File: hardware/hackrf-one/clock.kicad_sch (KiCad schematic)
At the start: 67 parts, among them P1 AD_CLK, P16 CLKIN, P2 CLKOUT, P21 MIX_CLK, P37 SCL, P38 SDA, P57 XCVR_CLK, P59 GCK2, P60 SGPIO_CLK, P72 GP_CLKIN, P8 FSX2_CLK, U16 74LVC1G3157, U19 Si5351A-B-GT, U22 74LVC1G80, U26 74AUP2G58GU, U27 74AUP2G58GU, U28 74AUP2G58GU, U29 74AUP2G58GU, X1 GSG-XTAL4PIN

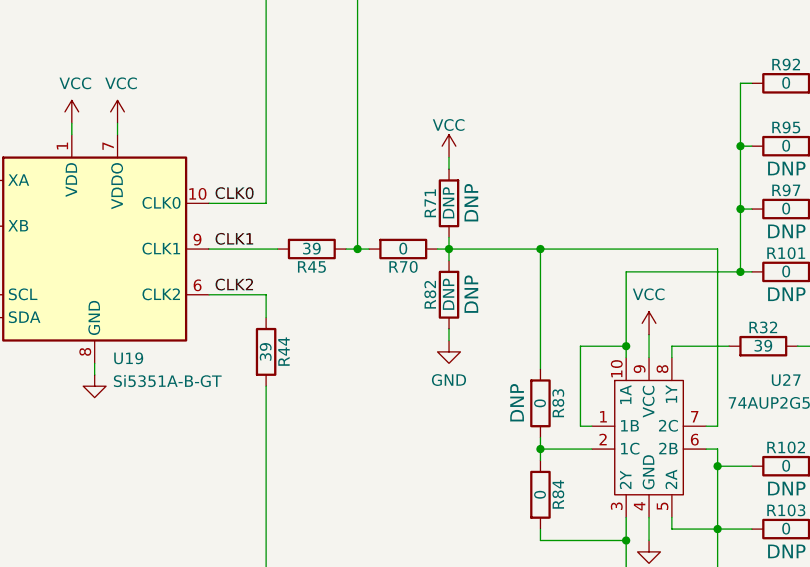
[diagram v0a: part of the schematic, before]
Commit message: HackRF One: adjust clock phase with RC delay
Remove chaining of buffers to delay GCK2 and instead use an RC delay for
both GCK2 and SGPIO_CLK.
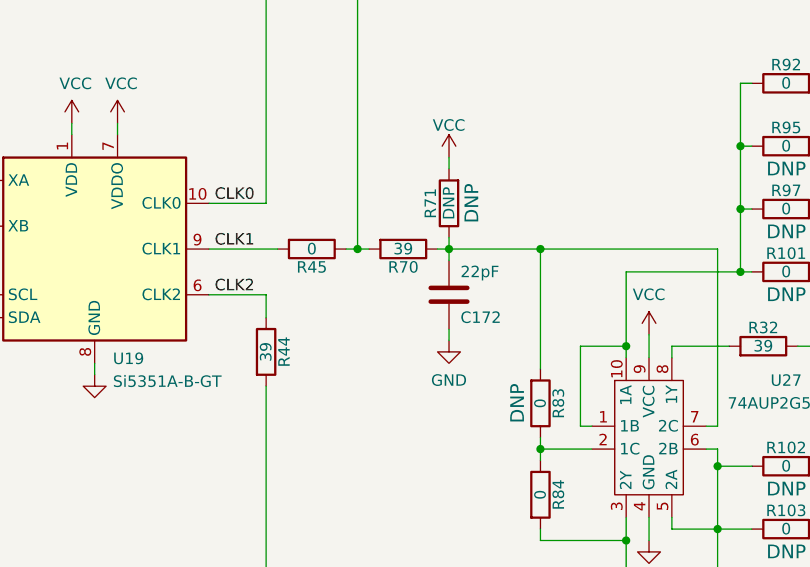
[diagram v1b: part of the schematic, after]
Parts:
- removed R82: DNP, hackrf:GSG-0402, symbol Device:R
- added C172: 22pF, hackrf:GSG-0402, symbol Device:C
- R45: value 39 -> 0; Part Number RMCF0402JT39R0 -> RMCF0402ZT0R00
- R70: value 0 -> 39; Part Number RMCF0402ZT0R00 -> RMCF0402JT39R0
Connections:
- net GND: now also C172.1
- net at R70.1, R71.1, R83.2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: now also C172.2
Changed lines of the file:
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@@
     (in_bom yes) (on_board yes)
     (property "Reference" "R70" (id 0) (at 272.415 94.107 90))
-    (property "Value" "0" (id 1) (at 272.415 92.075 90))
+    (property "Value" "39" (id 1) (at 272.415 92.075 90))
     (property "Footprint" "hackrf:GSG-0402" (id 2) (at 272.415 92.075 0)
       (effects (font (size 1.524 1.524)) hide)
@@
       (effects (font (size 1.524 1.524)) hide)
     )
-    (property "Part Number" "RMCF0402ZT0R00" (id 5) (at 272.415 92.075 0)
-      (effects (font (size 1.524 1.524)) hide)
-    )
-    (property "Description" "RES 0.0 OHM 1/16W 0402 SMD" (id 6) (at 272.415 92.075 0)
+    (property "Part Number" "RMCF0402JT39R0" (id 5) (at 272.415 92.075 0)
+      (effects (font (size 1.524 1.524)) hide)
+    )
+    (property "Description" "RES 39 OHM 1/16W 5% 0402 SMD" (id 6) (at 272.415 92.075 0)
       (effects (font (size 1.524 1.524)) hide)
     )
@@
     (in_bom yes) (on_board yes)
     (property "Reference" "R45" (id 0) (at 262.255 94.107 90))
-    (property "Value" "39" (id 1) (at 262.255 92.075 90))
+    (property "Value" "0" (id 1) (at 262.255 92.075 90))
     (property "Footprint" "hackrf:GSG-0402" (id 2) (at 262.255 92.075 0)
       (effects (font (size 1.524 1.524)) hide)
@@
       (effects (font (size 1.524 1.524)) hide)
     )
-    (property "Part Number" "RMCF0402JT39R0" (id 5) (at 262.255 92.075 0)
-      (effects (font (size 1.524 1.524)) hide)
-    )
-    (property "Description" "RES 39 OHM 1/16W 5% 0402 SMD" (id 6) (at 262.255 92.075 0)
+    (property "Part Number" "RMCF0402ZT0R00" (id 5) (at 262.255 92.075 0)
+      (effects (font (size 1.524 1.524)) hide)
+    )
+    (property "Description" "RES 0.0 OHM 1/16W 0402 SMD" (id 6) (at 262.255 92.075 0)
       (effects (font (size 1.524 1.524)) hide)
     )
@@
     (pin "1")
   )
-  (symbol (lib_id "Device:R") (at 277.495 97.155 180) (unit 1)
-    (in_bom yes) (on_board yes)
-    (property "Reference" "R82" (id 0) (at 275.463 97.155 90))
-    (property "Value" "DNP" (id 1) (at 277.495 97.155 90))
-    (property "Footprint" "hackrf:GSG-0402" (id 2) (at 277.495 97.155 0)
-      (effects (font (size 1.524 1.524)) hide)
-    )
-    (property "Datasheet" "" (id 3) (at 277.495 97.155 0)
-      (effects (font (size 1.524 1.524)))
-    )
-    (property "DNP" "DNP" (id 4) (at 280.035 97.155 90)
-      (effects (font (size 1.524 1.524)))
-    )
-    (pin "1")
-    (pin "2")
-  )
   (symbol (lib_id "Connector_Generic:Conn_01x01") (at 62.23 190.5 90) (unit 1)
     (in_bom yes) (on_board yes)
@@
     (pin "1")
   )
+  (symbol (lib_id "Device:C") (at 277.495 97.155 0) (mirror x) (unit 1)
+    (in_bom yes) (on_board yes)
+    (property "Reference" "C172" (id 0) (at 278.765 99.695 0)
+      (effects (font (size 1.27 1.27)) (justify left))
+    )
+    (property "Value" "22pF" (id 1) (at 278.765 94.615 0)
+      (effects (font (size 1.27 1.27)) (justify left))
+    )
+    (property "Footprint" "hackrf:GSG-0402" (id 2) (at 277.495 97.155 0)
+      (effects (font (size 1.524 1.524)) hide)
+    )
+    (property "Datasheet" "" (id 3) (at 277.495 97.155 0)
+      (effects (font (size 1.524 1.524)) hide)
+    )
+    (property "Manufacturer" "Samsung" (id 4) (at 286.385 100.965 0)
+      (effects (font (size 1.524 1.524)) hide)
+    )
+    (property "Part Number" "CL05C220JB5NNNC" (id 5) (at 286.385 100.965 0)
+      (effects (font (size 1.524 1.524)) hide)
+    )
+    (property "Description" "CAP CER 22PF 50V 5% C0G/NP0 0402" (id 6) (at 286.385 100.965 0)
+      (effects (font (size 1.524 1.524)) hide)
+    )
+    (pin "1")
+    (pin "2")
+  )
   (symbol (lib_id "Device:R") (at 101.6 81.28 0) (unit 1)

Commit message: HackRF One: update 100 nF capacitor part selection
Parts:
- C113, C119, C120, C121, C122, C159, C168, C68, C69: Manufacturer Murata -> Samsung; Part Number GRM155R61A104KA01D -> CL05A104KA5NNNC
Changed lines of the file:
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@@
       (effects (font (size 1.524 1.524)) hide)
     )
-    (property "Manufacturer" "Murata" (id 4) (at 90.805 224.79 0)
-      (effects (font (size 1.524 1.524)) hide)
-    )
-    (property "Part Number" "GRM155R61A104KA01D" (id 5) (at 90.805 224.79 0)
-      (effects (font (size 1.524 1.524)) hide)
-    )
-    (property "Description" "CAP CER 0.1UF 10V 10% X5R 0402" (id 6) (at 90.805 224.79 0)
+    (property "Manufacturer" "Samsung" (id 4) (at 90.805 224.79 0)
+      (effects (font (size 1.524 1.524)) hide)
+    )
+    (property "Part Number" "CL05A104KA5NNNC" (id 5) (at 90.805 224.79 0)
+      (effects (font (size 1.524 1.524)) hide)
+    )
+    (property "Description" "CAP CER 0.1UF 25V X5R 0402" (id 6) (at 90.805 224.79 0)
       (effects (font (size 1.524 1.524)) hide)
     )
@@
       (effects (font (size 1.524 1.524)) hide)
     )
-    (property "Manufacturer" "Murata" (id 4) (at 100.965 224.79 0)
-      (effects (font (size 1.524 1.524)) hide)
-    )
-    (property "Part Number" "GRM155R61A104KA01D" (id 5) (at 100.965 224.79 0)
-      (effects (font (size 1.524 1.524)) hide)
-    )
-    (property "Description" "CAP CER 0.1UF 10V 10% X5R 0402" (id 6) (at 100.965 224.79 0)
+    (property "Manufacturer" "Samsung" (id 4) (at 100.965 224.79 0)
+      (effects (font (size 1.524 1.524)) hide)
+    )
+    (property "Part Number" "CL05A104KA5NNNC" (id 5) (at 100.965 224.79 0)
+      (effects (font (size 1.524 1.524)) hide)
+    )
+    (property "Description" "CAP CER 0.1UF 25V X5R 0402" (id 6) (at 100.965 224.79 0)
       (effects (font (size 1.524 1.524)) hide)
     )
@@
       (effects (font (size 1.524 1.524)) hide)
     )
-    (property "Manufacturer" "Murata" (id 4) (at 111.125 224.79 0)
-      (effects (font (size 1.524 1.524)) hide)
-    )
-    (property "Part Number" "GRM155R61A104KA01D" (id 5) (at 111.125 224.79 0)
-      (effects (font (size 1.524 1.524)) hide)
-    )
-    (property "Description" "CAP CER 0.1UF 10V 10% X5R 0402" (id 6) (at 111.125 224.79 0)
+    (property "Manufacturer" "Samsung" (id 4) (at 111.125 224.79 0)
+      (effects (font (size 1.524 1.524)) hide)
+    )
+    (property "Part Number" "CL05A104KA5NNNC" (id 5) (at 111.125 224.79 0)
+      (effects (font (size 1.524 1.524)) hide)
+    )
+    (property "Description" "CAP CER 0.1UF 25V X5R 0402" (id 6) (at 111.125 224.79 0)
       (effects (font (size 1.524 1.524)) hide)
     )
@@
       (effects (font (size 1.524 1.524)) hide)
     )
-    (property "Manufacturer" "Murata" (id 4) (at 121.285 224.79 0)
-      (effects (font (size 1.524 1.524)) hide)
-    )
-    (property "Part Number" "GRM155R61A104KA01D" (id 5) (at 121.285 224.79 0)
-      (effects (font (size 1.524 1.524)) hide)
-    )
-    (property "Description" "CAP CER 0.1UF 10V 10% X5R 0402" (id 6) (at 121.285 224.79 0)
+    (property "Manufacturer" "Samsung" (id 4) (at 121.285 224.79 0)
+      (effects (font (size 1.524 1.524)) hide)
+    )
+    (property "Part Number" "CL05A104KA5NNNC" (id 5) (at 121.285 224.79 0)
+      (effects (font (size 1.524 1.524)) hide)
+    )
+    (property "Description" "CAP CER 0.1UF 25V X5R 0402" (id 6) (at 121.285 224.79 0)
       (effects (font (size 1.524 1.524)) hide)
     )
@@
       (effects (font (size 1.524 1.524)) hide)
     )
-    (property "Manufacturer" "Murata" (id 4) (at 131.445 224.79 0)
-      (effects (font (size 1.524 1.524)) hide)
-    )
-    (property "Part Number" "GRM155R61A104KA01D" (id 5) (at 131.445 224.79 0)
-      (effects (font (size 1.524 1.524)) hide)
-    )
-    (property "Description" "CAP CER 0.1UF 10V 10% X5R 0402" (id 6) (at 131.445 224.79 0)
+    (property "Manufacturer" "Samsung" (id 4) (at 131.445 224.79 0)
+      (effects (font (size 1.524 1.524)) hide)
+    )
+    (property "Part Number" "CL05A104KA5NNNC" (id 5) (at 131.445 224.79 0)
+      (effects (font (size 1.524 1.524)) hide)
+    )
+    (property "Description" "CAP CER 0.1UF 25V X5R 0402" (id 6) (at 131.445 224.79 0)
       (effects (font (size 1.524 1.524)) hide)
     )
@@
       (effects (font (size 1.524 1.524)) hide)
     )
-    (property "Manufacturer" "Murata" (id 4) (at 95.25 87.63 0)
-      (effects (font (size 1.524 1.524)) hide)
-    )
-    (property "Part Number" "GRM155R61A104KA01D" (id 5) (at 95.25 87.63 0)
-      (effects (font (size 1.524 1.524)) hide)
-    )
-    (property "Description" "CAP CER 0.1UF 10V 10% X5R 0402" (id 6) (at 95.25 87.63 0)
+    (property "Manufacturer" "Samsung" (id 4) (at 95.25 87.63 0)
+      (effects (font (size 1.524 1.524)) hide)
+    )
+    (property "Part Number" "CL05A104KA5NNNC" (id 5) (at 95.25 87.63 0)
+      (effects (font (size 1.524 1.524)) hide)
+    )
+    (property "Description" "CAP CER 0.1UF 25V X5R 0402" (id 6) (at 95.25 87.63 0)
       (effects (font (size 1.524 1.524)) hide)
     )
@@
       (effects (font (size 1.524 1.524)) hide)
     )
-    (property "Manufacturer" "Murata" (id 4) (at 70.485 224.79 0)
-      (effects (font (size 1.524 1.524)) hide)
-    )
-    (property "Part Number" "GRM155R61A104KA01D" (id 5) (at 70.485 224.79 0)
-      (effects (font (size 1.524 1.524)) hide)
-    )
-    (property "Description" "CAP CER 0.1UF 10V 10% X5R 0402" (id 6) (at 70.485 224.79 0)
+    (property "Manufacturer" "Samsung" (id 4) (at 70.485 224.79 0)
+      (effects (font (size 1.524 1.524)) hide)
+    )
+    (property "Part Number" "CL05A104KA5NNNC" (id 5) (at 70.485 224.79 0)
+      (effects (font (size 1.524 1.524)) hide)
+    )
+    (property "Description" "CAP CER 0.1UF 25V X5R 0402" (id 6) (at 70.485 224.79 0)
       (effects (font (size 1.524 1.524)) hide)
     )
@@
       (effects (font (size 1.524 1.524)) hide)
     )
-    (property "Manufacturer" "Murata" (id 4) (at 60.325 224.79 0)
-      (effects (font (size 1.524 1.524)) hide)
-    )
-    (property "Part Number" "GRM155R61A104KA01D" (id 5) (at 60.325 224.79 0)
-      (effects (font (size 1.524 1.524)) hide)
-    )
-    (property "Description" "CAP CER 0.1UF 10V 10% X5R 0402" (id 6) (at 60.325 224.79 0)
+    (property "Manufacturer" "Samsung" (id 4) (at 60.325 224.79 0)
+      (effects (font (size 1.524 1.524)) hide)
+    )
+    (property "Part Number" "CL05A104KA5NNNC" (id 5) (at 60.325 224.79 0)
+      (effects (font (size 1.524 1.524)) hide)
+    )
+    (property "Description" "CAP CER 0.1UF 25V X5R 0402" (id 6) (at 60.325 224.79 0)
       (effects (font (size 1.524 1.524)) hide)
     )
@@
       (effects (font (size 1.524 1.524)) hide)
     )
-    (property "Manufacturer" "Murata" (id 4) (at 80.645 224.79 0)
-      (effects (font (size 1.524 1.524)) hide)
-    )
-    (property "Part Number" "GRM155R61A104KA01D" (id 5) (at 80.645 224.79 0)
-      (effects (font (size 1.524 1.524)) hide)
-    )
-    (property "Description" "CAP CER 0.1UF 10V 10% X5R 0402" (id 6) (at 80.645 224.79 0)
-      (effects (font (size 1.524 1.524)) hide)
-    )
+    (property "Manufacturer" "Samsung" (id 4) (at 80.645 224.79 0)
+      (effects (font (size 1.524 1.524)) hide)
+    )
+    (property "Part Number" "CL05A104KA5NNNC" (id 5) (at 80.645 224.79 0)
+      (effects (font (size 1.524 1.524)) hide)
+    )
+    (property "Description" "CAP CER 0.1UF 25V X5R 0402" (id 6) (at 80.645 224.79 0)
+      (effects (font (size 1.524 1.524)) hide)
+    )

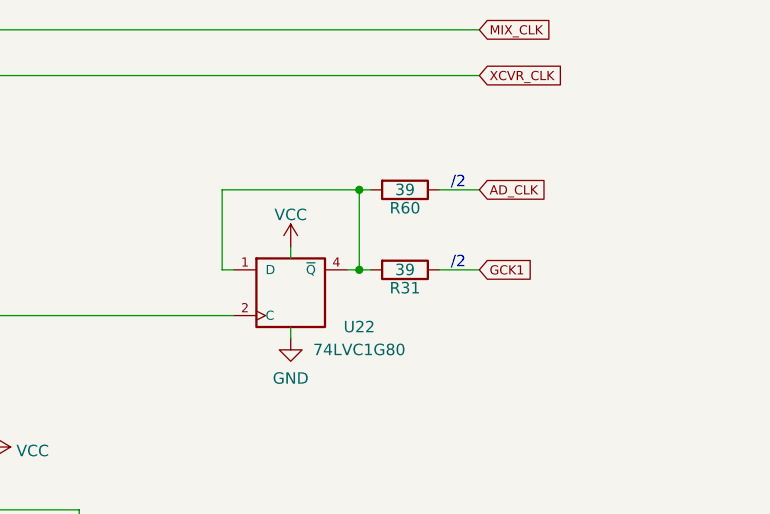
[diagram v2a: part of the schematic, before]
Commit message: HackRF One: update clock termination passives
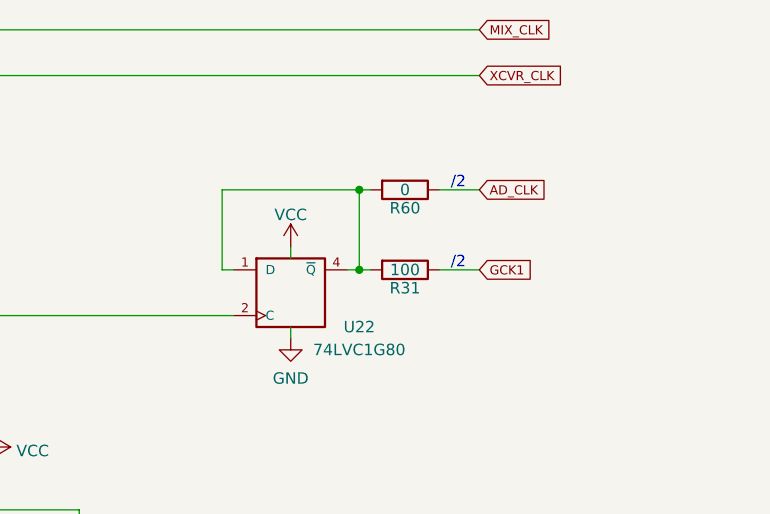
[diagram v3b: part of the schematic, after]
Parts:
- R31: value 39 -> 100; Manufacturer Stackpole -> Yageo; Part Number RMCF0402JT39R0 -> RC0402JR-07100RL
- R60: value 39 -> 0; Part Number RMCF0402JT39R0 -> RMCF0402ZT0R00
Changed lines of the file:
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@@
     (in_bom yes) (on_board yes)
     (property "Reference" "R31" (id 0) (at 366.395 56.007 90))
-    (property "Value" "39" (id 1) (at 366.395 53.975 90))
+    (property "Value" "100" (id 1) (at 366.395 53.975 90))
     (property "Footprint" "hackrf:GSG-0402" (id 2) (at 366.395 53.975 0)
       (effects (font (size 1.524 1.524)) hide)
@@
       (effects (font (size 1.524 1.524)) hide)
     )
-    (property "Manufacturer" "Stackpole" (id 4) (at 366.395 53.975 0)
-      (effects (font (size 1.524 1.524)) hide)
-    )
-    (property "Part Number" "RMCF0402JT39R0" (id 5) (at 366.395 53.975 0)
-      (effects (font (size 1.524 1.524)) hide)
-    )
-    (property "Description" "RES 39 OHM 1/16W 5% 0402 SMD" (id 6) (at 366.395 53.975 0)
+    (property "Manufacturer" "Yageo" (id 4) (at 366.395 53.975 0)
+      (effects (font (size 1.524 1.524)) hide)
+    )
+    (property "Part Number" "RC0402JR-07100RL" (id 5) (at 366.395 53.975 0)
+      (effects (font (size 1.524 1.524)) hide)
+    )
+    (property "Description" "RES 100 OHM 5% 1/16W 0402" (id 6) (at 366.395 53.975 0)
       (effects (font (size 1.524 1.524)) hide)
     )
@@
     (in_bom yes) (on_board yes)
     (property "Reference" "R60" (id 0) (at 366.395 47.117 90))
-    (property "Value" "39" (id 1) (at 366.395 45.085 90))
+    (property "Value" "0" (id 1) (at 366.395 45.085 90))
     (property "Footprint" "hackrf:GSG-0402" (id 2) (at 366.395 45.085 0)
       (effects (font (size 1.524 1.524)) hide)
@@
       (effects (font (size 1.524 1.524)) hide)
     )
-    (property "Part Number" "RMCF0402JT39R0" (id 5) (at 366.395 45.085 0)
-      (effects (font (size 1.524 1.524)) hide)
-    )
-    (property "Description" "RES 39 OHM 1/16W 5% 0402 SMD" (id 6) (at 366.395 45.085 0)
-      (effects (font (size 1.524 1.524)) hide)
-    )
+    (property "Part Number" "RMCF0402ZT0R00" (id 5) (at 366.395 45.085 0)
+      (effects (font (size 1.524 1.524)) hide)
+    )
+    (property "Description" "RES 0.0 OHM 1/16W 0402 SMD" (id 6) (at 366.395 45.085 0)
+      (effects (font (size 1.524 1.524)) hide)
+    )

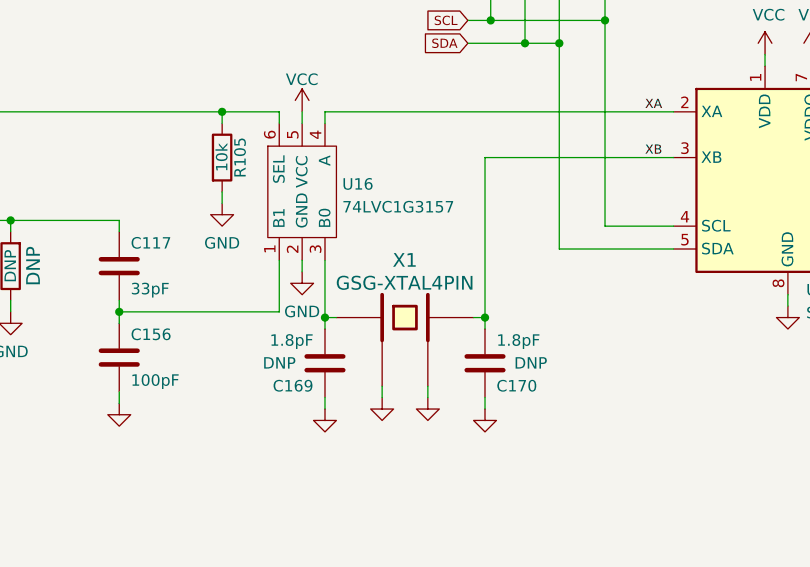
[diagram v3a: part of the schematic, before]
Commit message: HackRF One: clean up
- silkscreen
- fabrication attributes
- dates
- copyright
- README
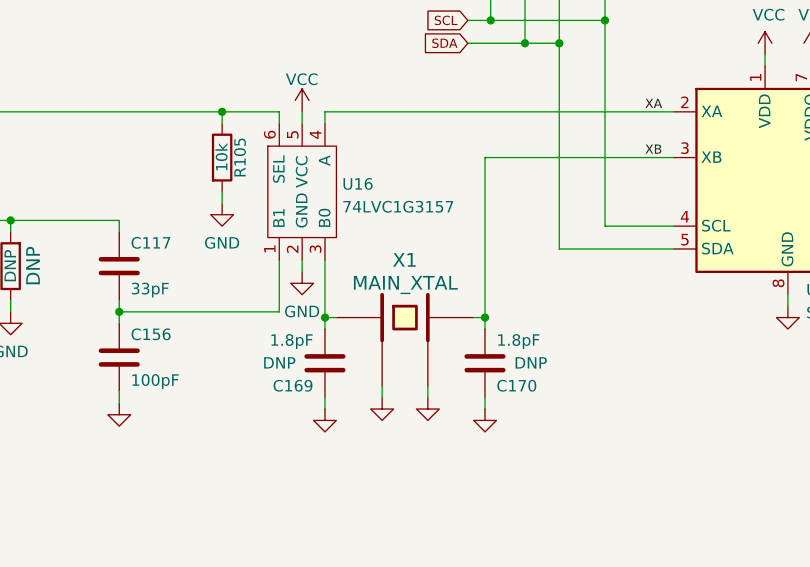
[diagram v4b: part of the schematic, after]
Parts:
- X1: value GSG-XTAL4PIN -> MAIN_XTAL
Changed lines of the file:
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@@
   (title_block
     (title "HackRF One")
-    (date "2022-08-29")
+    (date "2022-10-30")
     (rev "r9")
     (company "Copyright 2012-2022 Great Scott Gadgets")
-    (comment 1 "Michael Ossmann")
-    (comment 2 "Licensed under the CERN-OHL-P v2")
+    (comment 1 "Licensed under the CERN-OHL-P v2")
   )
   (junction (at 257.175 167.64) (diameter 0) (color 0 0 0 0)
@@
       (effects (font (size 1.524 1.524)))
     )
-    (property "Value" "GSG-XTAL4PIN" (id 1) (at 195.58 103.505 0)
+    (property "Value" "MAIN_XTAL" (id 1) (at 195.58 103.505 0)
       (effects (font (size 1.524 1.524)))
     )

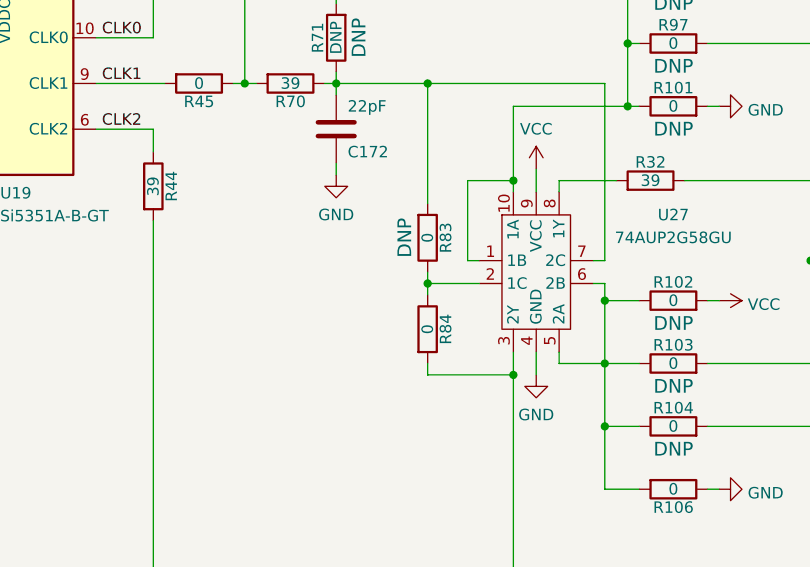
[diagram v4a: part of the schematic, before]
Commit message: HackRF One: populate R83 instead of R84
This removes clock buffer chaining which was intended to be done when
the RC delay was added.
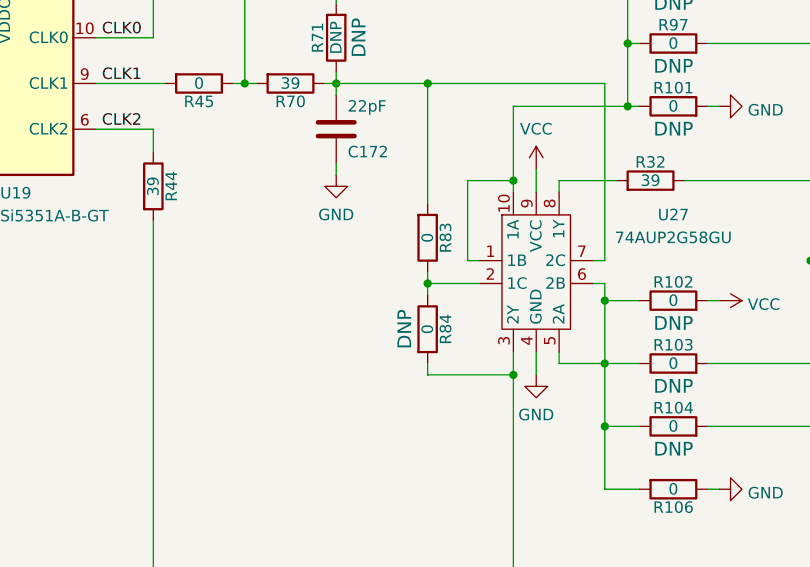
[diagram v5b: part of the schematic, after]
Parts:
- R83: DNP DNP -> (none)
- R84: DNP (none) -> DNP
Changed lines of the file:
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@@
       (effects (font (size 1.524 1.524)) hide)
-    )
-    (property "DNP" "DNP" (id 7) (at 285.115 109.22 90)
-      (effects (font (size 1.524 1.524)))
     )
     (pin "1")
@@
       (effects (font (size 1.524 1.524)) hide)
     )
-    (pin "1")
+    (property "DNP" "DNP" (id 7) (at 285.115 119.38 90)
+      (effects (font (size 1.524 1.524)))
+    )
+    (pin "1")
